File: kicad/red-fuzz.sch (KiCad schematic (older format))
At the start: 37 parts, among them J1 2.1mm Center Neg Insulated, J2 Input Stereo, J3 TEST_1P, J4 TEST_1P, J5 TEST_1P, J6 Output Mono, Q1 j201, SW1 SW_3PDT, SW2 SW_SPDT, U1 NE5532

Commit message: Project Rev. B
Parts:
- C1: footprint Capacitors_THT:CP_Radial_D10.0mm_P3.50mm -> Capacitors_THT:CP_Radial_D5.0mm_P2.50mm
- C8: footprint Capacitors_THT:CP_Radial_D10.0mm_P2.50mm -> Capacitors_THT:CP_Radial_D5.0mm_P2.50mm
- J2: footprint Connectors:NMJ6HCD2 -> Pin_Headers:Pin_Header_Straight_1x03_Pitch2.54mm
- J6: footprint Connectors:NMJ6HCD2 -> Pin_Headers:Pin_Header_Straight_1x02_Pitch2.54mm
- RV1, RV2, RV3: footprint guitar-projects:pot_16mm_long_lead -> feetprints:pot_16mm_long_lead
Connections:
- net GND: no longer J2.5
- net at C3.1, R3.1, R4.2: now also U1.5 (+); no longer U1.3 (+)
- net at R5.1, R6.2, SW2.2 (B): now also U1.6 (-); no longer U1.2 (-)
- net at C5.2, D3.2 (A), D4.1 (K)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: now also U1.7; no longer U1.1
- net at J4.1: now also U1.3 (+); no longer U1.5 (+)
- net at J3.1: now also U1.2 (-); no longer U1.6 (-)
- net at J5.1: now also U1.1; no longer U1.7
- no-connect marks 1 -> 2
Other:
- note added: "LED 1.8V drop"
- note removed: "Connect board ground to\nbody of volume pot here\nto ground the chassis."
- moved on the sheet: R8
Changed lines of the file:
@@
 encoding utf-8
 Sheet 1 1
-Title "Red Fuzz "
+Title "Firemace"
 Date "2018-01-12"
 Rev "A"
 Comp "Cal Poly AES"
-Comment1 "Original Design by Robin Tomtlund"
-Comment2 "This based on source material from generalguitargadgets.com"
+Comment1 "This based on \"Red Fuzz\" from generalguitargadgets.com"
+Comment2 "Original Design \"Red Fuzz\"by Robin Tomtlund"
 Comment3 ""
 Comment4 ""
@@
 F 0 "RV1" V 5275 4800 50  0000 C CNN
 F 1 "1M Log" V 5350 4800 50  0000 C CNN
-F 2 "guitar-projects:pot_16mm_long_lead" H 5450 4800 50  0001 C CNN
+F 2 "feetprints:pot_16mm_long_lead" H 5450 4800 50  0001 C CNN
 F 3 "" H 5450 4800 50  0001 C CNN
 	1    5450 4800
@@
 F 0 "RV2" V 6475 4150 50  0000 C CNN
 F 1 "100k Lin" V 6550 4150 50  0000 C CNN
-F 2 "guitar-projects:pot_16mm_long_lead" H 6650 4150 50  0001 C CNN
+F 2 "feetprints:pot_16mm_long_lead" H 6650 4150 50  0001 C CNN
 F 3 "" H 6650 4150 50  0001 C CNN
 	1    6650 4150
@@
 L R R8
 U 1 1 5A59AF79
-P 8100 4400
-F 0 "R8" V 8180 4400 50  0000 C CNN
-F 1 "1M" V 8100 4400 50  0000 C CNN
-F 2 "Resistors_THT:R_Axial_DIN0207_L6.3mm_D2.5mm_P10.16mm_Horizontal" V 8030 4400 50  0001 C CNN
-F 3 "" H 8100 4400 50  0001 C CNN
-	1    8100 4400
+P 8100 4500
+F 0 "R8" V 8180 4500 50  0000 C CNN
+F 1 "1M" V 8100 4500 50  0000 C CNN
+F 2 "Resistors_THT:R_Axial_DIN0207_L6.3mm_D2.5mm_P10.16mm_Horizontal" V 8030 4500 50  0001 C CNN
+F 3 "" H 8100 4500 50  0001 C CNN
+	1    8100 4500
 	1    0    0    -1
 $EndComp
@@
 F 0 "C8" H 8925 4550 50  0000 L CNN
 F 1 "10u" H 8925 4350 50  0000 L CNN
-F 2 "Capacitors_THT:CP_Radial_D10.0mm_P2.50mm" H 8900 4450 50  0001 C CNN
+F 2 "Capacitors_THT:CP_Radial_D5.0mm_P2.50mm" H 8900 4450 50  0001 C CNN
 F 3 "" H 8900 4450 50  0001 C CNN
 	1    8900 4450
@@
 F 0 "RV3" V 9125 4700 50  0000 C CNN
 F 1 "100k Log" V 9200 4700 50  0000 C CNN
-F 2 "guitar-projects:pot_16mm_long_lead" H 9300 4700 50  0001 C CNN
+F 2 "feetprints:pot_16mm_long_lead" H 9300 4700 50  0001 C CNN
 F 3 "" H 9300 4700 50  0001 C CNN
 	1    9300 4700
@@
 F 0 "C1" H 2725 3050 50  0000 L CNN
 F 1 "100u" H 2725 2850 50  0000 L CNN
-F 2 "Capacitors_THT:CP_Radial_D10.0mm_P3.50mm" H 2700 2950 50  0001 C CNN
+F 2 "Capacitors_THT:CP_Radial_D5.0mm_P2.50mm" H 2700 2950 50  0001 C CNN
 F 3 "" H 2700 2950 50  0001 C CNN
 	1    2700 2950
@@
 $Comp
 L NE5532 U1
-U 1 1 5A5AB169
+U 2 1 5A5AB169
 P 4950 4150
 F 0 "U1" H 4950 4350 50  0000 L CNN
@@
 F 2 "Housings_DIP:DIP-8_W7.62mm_Socket_LongPads" H 4950 4150 50  0001 C CNN
 F 3 "" H 4950 4150 50  0001 C CNN
-	1    4950 4150
+	2    4950 4150
 	1    0    0    -1
 $EndComp
@@
 	5950 5450 5850 5450
 Wire Wire Line
-	5600 4800 5950 4800
-Wire Wire Line
 	5450 4950 5450 5000
 Wire Wire Line
@@
 	7850 4150 8200 4150
 Wire Wire Line
-	8100 4150 8100 4250
+	8100 4150 8100 4350
 Connection ~ 8100 4150
 Wire Wire Line
-	8100 4950 8100 4550
+	8100 4950 8100 4650
 Wire Wire Line
 	8500 3800 8500 3950
@@
 $Comp
 L NE5532 U1
-U 2 1 5A5AD326
+U 1 1 5A5AD326
 P 7100 1750
 F 0 "U1" H 7100 1950 50  0000 L CNN
@@
 F 2 "Housings_DIP:DIP-8_W7.62mm_Socket_LongPads" H 7100 1750 50  0001 C CNN
 F 3 "" H 7100 1750 50  0001 C CNN
-	2    7100 1750
+	1    7100 1750
 	1    0    0    -1
 $EndComp
@@
 Wire Wire Line
 	6700 1650 6700 1550
-Text Notes 8900 5550 0    60   ~ 0
-Connect board ground to\nbody of volume pot here\nto ground the chassis.
 Wire Wire Line
 	9500 4900 9500 6350
 Wire Wire Line
 	9500 6350 2400 6350
-Connection ~ 9100 4950
-Wire Wire Line
-	9100 5050 9100 4950
-$Comp
-L GNDPWR #PWR014
-U 1 1 5A5AFAD8
-P 9100 5050
-F 0 "#PWR014" H 9100 4850 50  0001 C CNN
-F 1 "GNDPWR" H 9100 4920 50  0000 C CNN
-F 2 "" H 9100 5000 50  0001 C CNN
-F 3 "" H 9100 5000 50  0001 C CNN
-	1    9100 5050
-	1    0    0    -1
-$EndComp
 $Comp
 L Audio-Jack-3_3Switches J2
@@
 F 0 "J2" H 1600 4250 50  0000 C CNN
 F 1 "Input Stereo" H 1650 3550 50  0000 C CNN
-F 2 "Connectors:NMJ6HCD2" H 1900 4050 50  0001 C CNN
+F 2 "Pin_Headers:Pin_Header_Straight_1x03_Pitch2.54mm" H 1900 4050 50  0001 C CNN
 F 3 "" H 1900 4050 50  0001 C CNN
 	1    1650 3950
@@
 	1950 3750 1950 4300
 $Comp
-L GND #PWR015
+L GND #PWR014
 U 1 1 5A5B15B6
 P 1950 4300
-F 0 "#PWR015" H 1950 4050 50  0001 C CNN
+F 0 "#PWR014" H 1950 4050 50  0001 C CNN
 F 1 "GND" H 1950 4150 50  0000 C CNN
 F 2 "" H 1950 4300 50  0001 C CNN
@@
 	1950 4250 1850 4250
 Connection ~ 1950 4250
-Wire Wire Line
-	1850 4050 1950 4050
-Connection ~ 1950 4050
 Wire Wire Line
 	1850 3850 1950 3850
@@
 F 0 "J6" H 10400 5300 50  0000 C CNN
 F 1 "Output Mono" H 10450 4600 50  0000 C CNN
-F 2 "Connectors:NMJ6HCD2" H 10700 5100 50  0001 C CNN
+F 2 "Pin_Headers:Pin_Header_Straight_1x02_Pitch2.54mm" H 10700 5100 50  0001 C CNN
 F 3 "" H 10700 5100 50  0001 C CNN
 	1    10450 5000
@@
 Connection ~ 10150 5000
 $Comp
-L GND #PWR016
+L GND #PWR015
 U 1 1 5A5B303B
 P 10150 5300
-F 0 "#PWR016" H 10150 5050 50  0001 C CNN
+F 0 "#PWR015" H 10150 5050 50  0001 C CNN
 F 1 "GND" H 10150 5150 50  0000 C CNN
 F 2 "" H 10150 5300 50  0001 C CNN
@@
 Additional opamp section \navailable for mods.
 $Comp
-L GND #PWR017
+L GND #PWR016
 U 1 1 5A5B36D4
 P 1950 3050
-F 0 "#PWR017" H 1950 2800 50  0001 C CNN
+F 0 "#PWR016" H 1950 2800 50  0001 C CNN
 F 1 "GND" H 1950 2900 50  0000 C CNN
 F 2 "" H 1950 3050 50  0001 C CNN
@@
 Wire Wire Line
 	1950 2950 1850 2950
-Text Label 2000 2850 0    60   ~ 0
+Text Label 2250 3100 0    60   ~ 0
 Batt+
-Text Label 2000 3950 0    60   ~ 0
+Text Label 2250 3700 0    60   ~ 0
 Batt-
+Wire Wire Line
+	5600 4800 5950 4800
+Text Notes 3650 3200 1    60   ~ 0
+LED 1.8V drop
+NoConn ~ 1850 4050
 $EndSCHEMATC

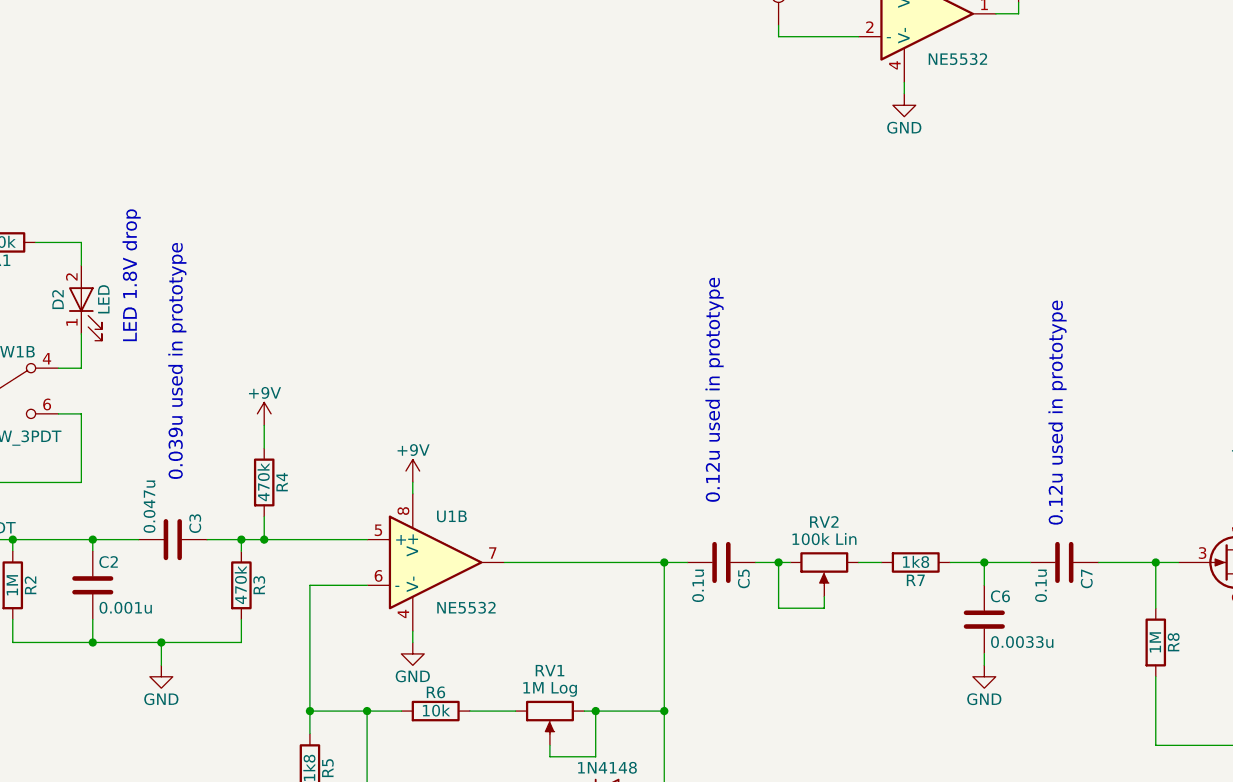
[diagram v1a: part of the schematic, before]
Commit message: minor changes to match available supply. Add new BOM.
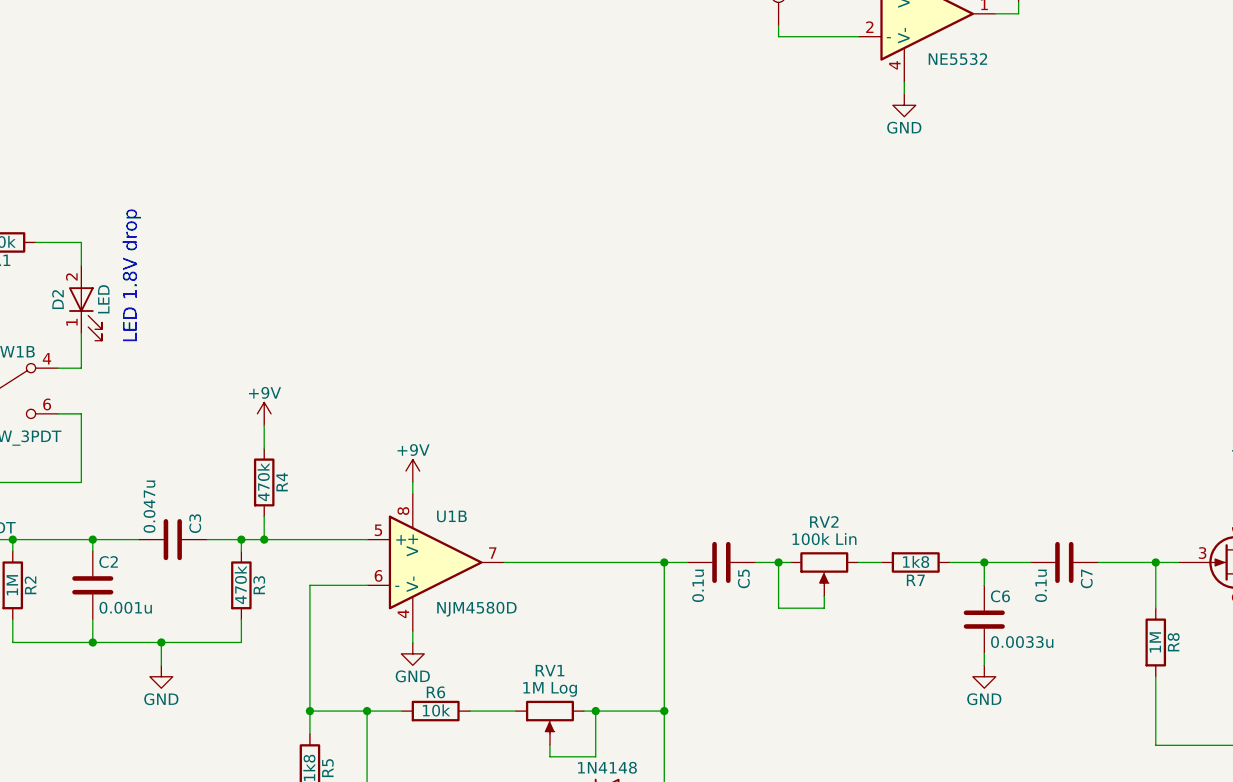
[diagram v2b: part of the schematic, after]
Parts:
- U1: value NE5532 -> NJM4580D
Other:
- note removed: "0.039u used in prototype"
- note removed: "0.12u used in prototype"
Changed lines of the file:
@@
 LIBS:valves
 LIBS:guitar-pedals
+LIBS:dk_Addressable-Specialty
+LIBS:dk_Alarms-Buzzers-and-Sirens
+LIBS:dk_Automotive-Relays
+LIBS:dk_Balun
+LIBS:dk_Barrel-Audio-Connectors
+LIBS:dk_Battery-Holders-Clips-Contacts
+LIBS:dk_Clock-Timing-Clock-Generators-PLLs-Frequency-Synthesizers
+LIBS:dk_Clock-Timing-Programmable-Timers-and-Oscillators
+LIBS:dk_Clock-Timing-Real-Time-Clocks
+LIBS:dk_Coaxial-Connectors-(RF)
+LIBS:dk_Current-Transducers
+LIBS:dk_Data-Acquisition-ADCs-DACs-Special-Purpose
+LIBS:dk_Data-Acquisition-Analog-to-Digital-Converters-(ADC)
+LIBS:dk_Data-Acquisition-Digital-Potentiometers
+LIBS:dk_Data-Acquisition-Digital-to-Analog-Converters-(DAC)
+LIBS:dk_Data-Acquisition-Touch-Screen-Controllers
+LIBS:dk_DC-DC-Converters
+LIBS:dk_Digital-Isolators
+LIBS:dk_Diodes-Bridge-Rectifiers
+LIBS:dk_Diodes-Rectifiers-Arrays
+LIBS:dk_Diodes-Rectifiers-Single
+LIBS:dk_Diodes-Zener-Single
+LIBS:dk_Display-Modules-LED-Character-and-Numeric
+LIBS:dk_D-Sub-Connectors
+LIBS:dk_Embedded-Microcontrollers
+LIBS:dk_Encoders
+LIBS:dk_Evaluation-Boards-Sensors
+LIBS:dk_Ferrite-Beads-and-Chips
+LIBS:dk_Fixed-Inductors
+LIBS:dk_Fuses
+LIBS:dk_Gas-Sensors
+LIBS:dk_Humidity-Moisture-Sensors
+LIBS:dk_Image-Sensors-Camera
+LIBS:dk_Infrared-UV-Visible-Emitters
+LIBS:dk_Inrush-Current-Limiters-(ICL)
+LIBS:dk_Interface-Analog-Switches-Multiplexers-Demultiplexers
+LIBS:dk_Interface-Analog-Switches-Special-Purpose
+LIBS:dk_Interface-Controllers
+LIBS:dk_Interface-Drivers-Receivers-Transceivers
+LIBS:dk_Interface-I-O-Expanders
+LIBS:dk_Interface-Modules
+LIBS:dk_Interface-Sensor-and-Detector-Interfaces
+LIBS:dk_Interface-Sensor-Capacitive-Touch
+LIBS:dk_Interface-Specialized
+LIBS:dk_LED-Indication-Discrete
+LIBS:dk_LEDs-Circuit-Board-Indicators-Arrays-Light-Bars-Bar-Graphs
 LIBS:dk_Linear-Amplifiers-Audio
-LIBS:dk_Linear-Amplifiers-Instrumentation_OP_Amps_Buffer_Amps
-LIBS:dk_Barrel-Audio_Connectors
+LIBS:dk_Linear-Amplifiers-Instrumentation-OP-Amps-Buffer-Amps
+LIBS:dk_Linear-Comparators
+LIBS:dk_Logic-Buffers-Drivers-Receivers-Transceivers
+LIBS:dk_Logic-Flip-Flops
+LIBS:dk_Logic-Gates-and-Inverters
+LIBS:dk_Logic-Multivibrators
+LIBS:dk_Logic-Shift-Registers
+LIBS:dk_Logic-Signal-Switches-Multiplexers-Decoders
+LIBS:dk_Logic-Translators-Level-Shifters
+LIBS:dk_Magnetic-Sensors-Compass-Magnetic-Field-(Modules)
+LIBS:dk_Magnetic-Sensors-Linear-Compass-(ICs)
+LIBS:dk_Magnetic-Sensors-Switches-(Solid-State)
+LIBS:dk_Memory
+LIBS:dk_Memory-Connectors-PC-Card-Sockets
+LIBS:dk_Microphones
+LIBS:dk_Modular-Connectors-Jacks
+LIBS:dk_Modular-Connectors-Jacks-With-Magnetics
+LIBS:dk_Motion-Sensors-Accelerometers
+LIBS:dk_Motion-Sensors-IMUs-(Inertial-Measurement-Units)
+LIBS:dk_Motion-Sensors-Tilt-Switches
+LIBS:dk_Navigation-Switches-Joystick
+LIBS:dk_Optical-Sensors-Ambient-Light-IR-UV-Sensors
+LIBS:dk_Optical-Sensors-Photo-Detectors-Remote-Receiver
+LIBS:dk_Optical-Sensors-Photodiodes
+LIBS:dk_Optical-Sensors-Phototransistors
+LIBS:dk_Optical-Sensors-Reflective-Analog-Output
+LIBS:dk_Optoisolators-Logic-Output
+LIBS:dk_Optoisolators-Transistor-Photovoltaic-Output
+LIBS:dk_Optoisolators-Triac-SCR-Output
+LIBS:dk_Oscillators
+LIBS:dk_PMIC-AC-DC-Converters-Offline-Switchers
+LIBS:dk_PMIC-Battery-Chargers
+LIBS:dk_PMIC-Battery-Management
+LIBS:dk_PMIC-Current-Regulation-Management
+LIBS:dk_PMIC-Full-Half-Bridge-Drivers
+LIBS:dk_PMIC-Gate-Drivers
+LIBS:dk_PMIC-LED-Drivers
+LIBS:dk_PMIC-Motor-Drivers-Controllers
+LIBS:dk_PMIC-OR-Controllers-Ideal-Diodes
+LIBS:dk_PMIC-Power-Distribution-Switches-Load-Drivers
+LIBS:dk_PMIC-Power-Management-Specialized
+LIBS:dk_PMIC-RMS-to-DC-Converters
+LIBS:dk_PMIC-Supervisors
+LIBS:dk_PMIC-Thermal-Management
+LIBS:dk_PMIC-V-F-and-F-V-Converters
+LIBS:dk_PMIC-Voltage-Reference
+LIBS:dk_PMIC-Voltage-Regulators-DC-DC-Switching-Controllers
+LIBS:dk_PMIC-Voltage-Regulators-DC-DC-Switching-Regulators
+LIBS:dk_PMIC-Voltage-Regulators-Linear
+LIBS:dk_PMIC-Voltage-Regulators-Special-Purpose
+LIBS:dk_Power-Relays-Over-2-Amps
+LIBS:dk_Pressure-Sensors-Transducers
+LIBS:dk_Programmable-Oscillators
+LIBS:dk_Pushbutton-Switches
+LIBS:dk_Rectangular-Connectors-Headers-Male-Pins
+LIBS:dk_Reed-Relays
+LIBS:dk_Resistor-Networks-Arrays
+LIBS:dk_RF-Amplifiers
+LIBS:dk_RF-Antennas
+LIBS:dk_RF-Demodulators
+LIBS:dk_RF-Detectors
+LIBS:dk_RF-Evaluation-and-Development-Kits-Boards
+LIBS:dk_RFID-RF-Access-Monitoring-ICs
+LIBS:dk_RF-Receivers
+LIBS:dk_RF-Switches
+LIBS:dk_RF-Transceiver-ICs
+LIBS:dk_RF-Transceiver-Modules
+LIBS:dk_RF-Transmitters
+LIBS:dk_Rotary-Potentiometers-Rheostats
+LIBS:dk_Sensors-Transducers_Accessories
+LIBS:dk_Signal-Relays-Up-to-2-Amps
+LIBS:dk_Slide-Switches
+LIBS:dk_Solid-State-Relays
+LIBS:dk_Specialized-ICs
+LIBS:dk_Specialized-Sensors
+LIBS:dk_Surge-Suppression-ICs
+LIBS:dk_Tactile-Switches
+LIBS:dk_Temperature-Sensors-Analog-and-Digital-Output
+LIBS:dk_Thermal-Cutoffs-(Thermal-Fuses)
+LIBS:dk_Thyristors-DIACs-SIDACs
+LIBS:dk_Thyristors-SCRs
+LIBS:dk_Thyristors-TRIACs
+LIBS:dk_Toggle-Switches
+LIBS:dk_Transistors-Bipolar-(BJT)-Arrays
+LIBS:dk_Transistors-Bipolar-(BJT)-RF
+LIBS:dk_Transistors-Bipolar-(BJT)-Single
+LIBS:dk_Transistors-Bipolar-(BJT)-Single-Pre-Biased
+LIBS:dk_Transistors-FETs-MOSFETs-Arrays
+LIBS:dk_Transistors-FETs-MOSFETs-RF
+LIBS:dk_Transistors-FETs-MOSFETs-Single
+LIBS:dk_Transistors-JFETs
+LIBS:dk_Trimmer-Potentiometers
+LIBS:dk_TVS-Diodes
+LIBS:dk_TVS-Mixed-Technology
+LIBS:dk_USB-DVI-HDMI-Connectors
 LIBS:red-fuzz-cache
 EELAYER 25 0
@@
 P 4950 4150
 F 0 "U1" H 4950 4350 50  0000 L CNN
-F 1 "NE5532" H 4950 3950 50  0000 L CNN
+F 1 "NJM4580D" H 4950 3950 50  0000 L CNN
 F 2 "Housings_DIP:DIP-8_W7.62mm_Socket_LongPads" H 4950 4150 50  0001 C CNN
 F 3 "" H 4950 4150 50  0001 C CNN
@@
 	1    0    0    -1
 $EndComp
-Text Notes 7700 4000 1    60   ~ 0
-0.12u used in prototype
-Text Notes 6200 3900 1    60   ~ 0
-0.12u used in prototype
-Text Notes 3850 3800 1    60   ~ 0
-0.039u used in prototype
 Text Notes 6650 1200 0    60   ~ 0
 Additional opamp section \navailable for mods.
